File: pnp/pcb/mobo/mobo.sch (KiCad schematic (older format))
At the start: 19 parts, among them SW2 RESET

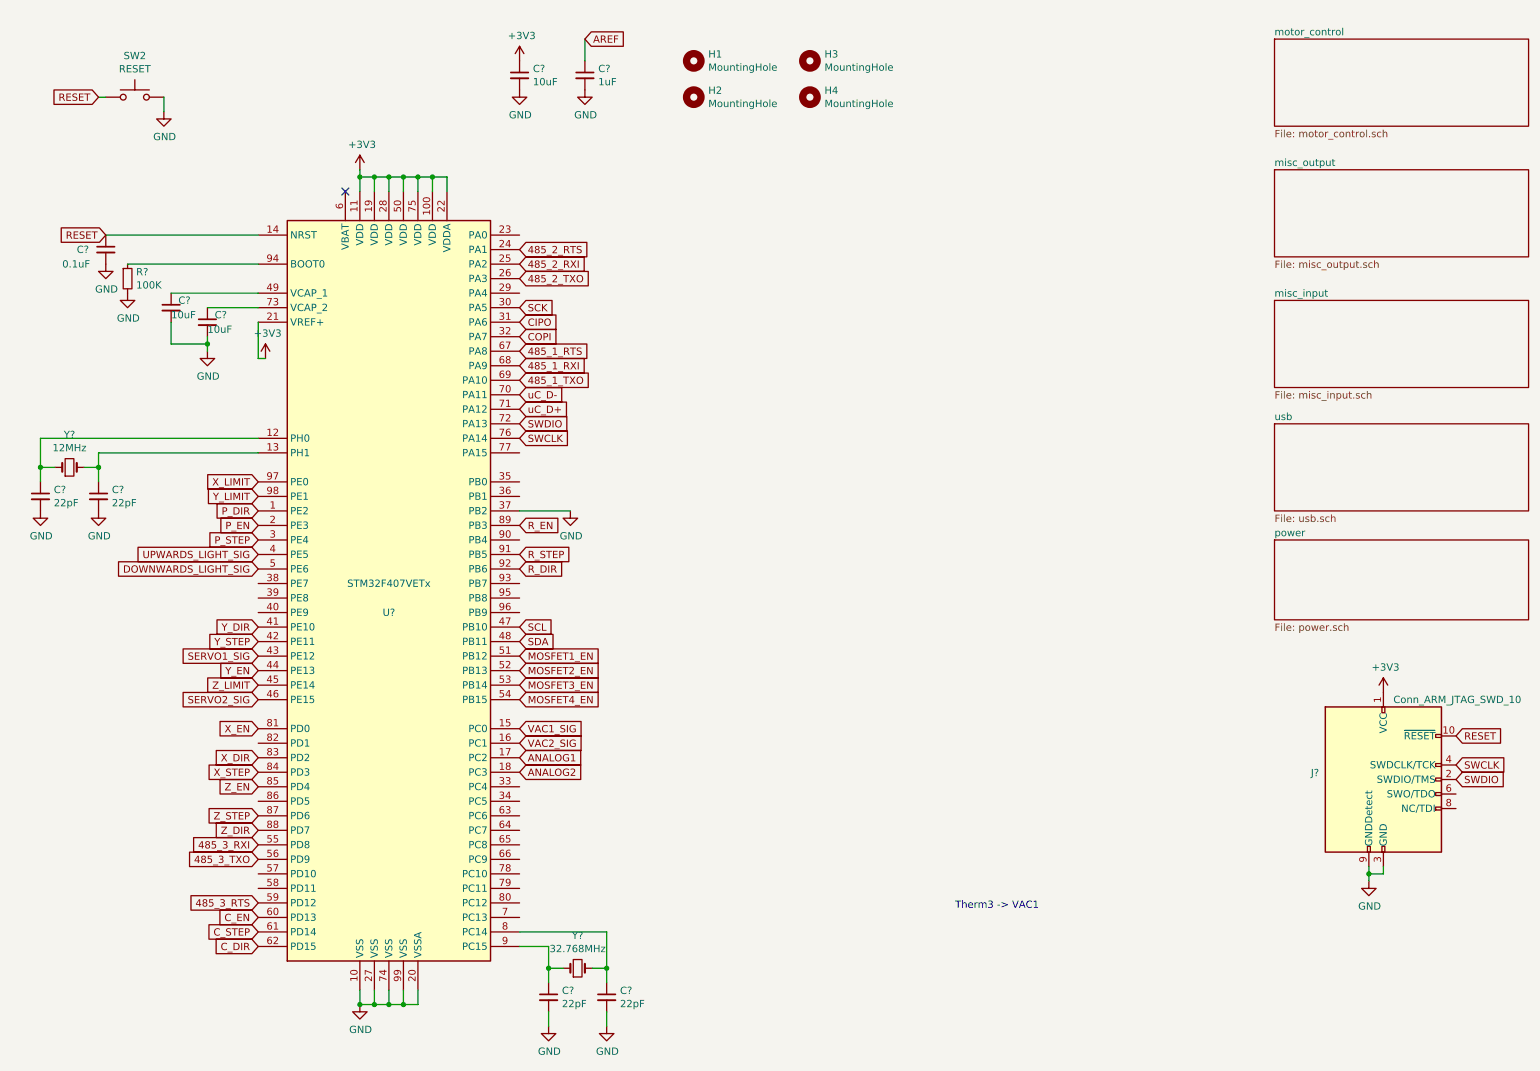
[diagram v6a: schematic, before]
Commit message: added spi to motor drivers
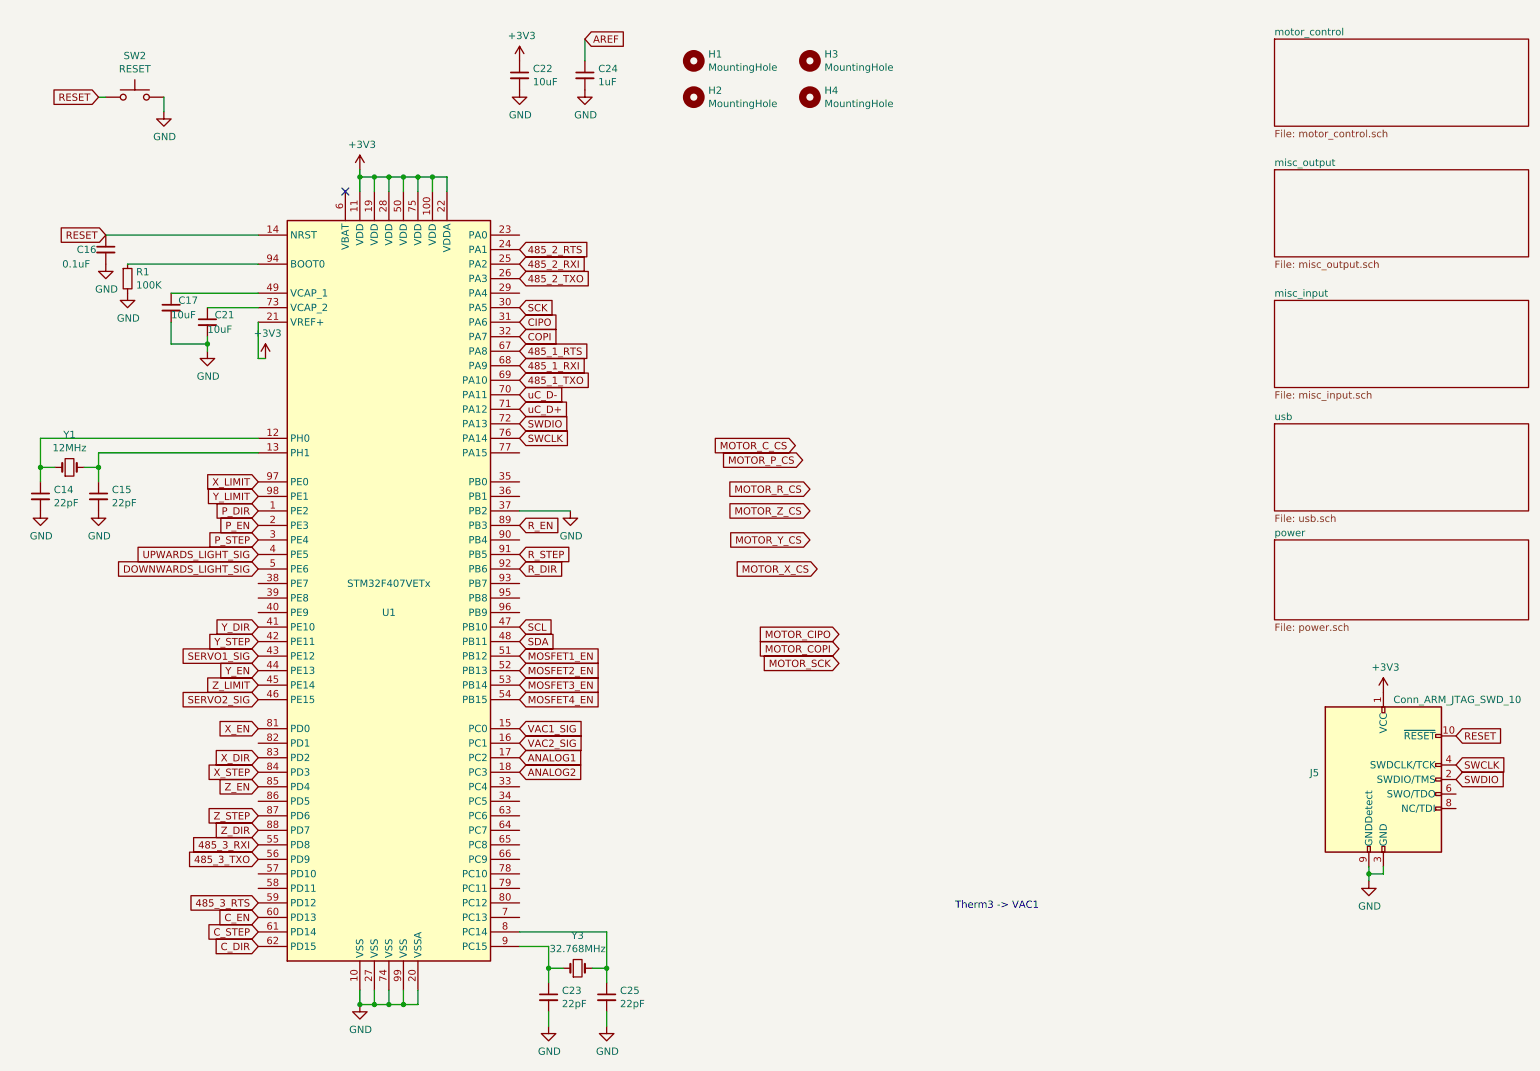
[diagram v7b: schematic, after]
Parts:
- R1: renamed from R?; footprint (none) -> Resistor_SMD:R_0805_2012Metric_Pad1.15x1.40mm_HandSolder
- Y1, Y3: renamed from Y?; footprint (none) -> Crystal:Crystal_SMD_0603-2Pin_6.0x3.5mm
- gave numbers to parts that had none: 11
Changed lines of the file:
@@
 R_EN
 $Comp
-L mobo-rescue:Conn_ARM_JTAG_SWD_10-Connector J?
+L mobo-rescue:Conn_ARM_JTAG_SWD_10-Connector J5
 U 1 1 5EEECA88
 P 9950 5750
-F 0 "J?" H 9507 5796 50  0000 R CNN
+F 0 "J5" H 9507 5796 50  0000 R CNN
 F 1 "Conn_ARM_JTAG_SWD_10" H 10900 6300 50  0000 R CNN
 F 2 "Connector_PinHeader_1.27mm:PinHeader_2x05_P1.27mm_Vertical_SMD" H 10000 5200 50  0001 L TNN
@@
 $EndComp
 $Comp
-L power:+3V3 #PWR?
+L power:+3V3 #PWR0114
 U 1 1 5EEF09A3
 P 2900 1550
-F 0 "#PWR?" H 2900 1400 50  0001 C CNN
+F 0 "#PWR0114" H 2900 1400 50  0001 C CNN
 F 1 "+3V3" H 2915 1723 50  0000 C CNN
 F 2 "" H 2900 1550 50  0001 C CNN
@@
 SWDIO
 $Comp
-L power:+3V3 #PWR?
+L power:+3V3 #PWR0115
 U 1 1 5EF002D9
 P 9950 5150
-F 0 "#PWR?" H 9950 5000 50  0001 C CNN
+F 0 "#PWR0115" H 9950 5000 50  0001 C CNN
 F 1 "+3V3" H 9965 5323 50  0000 C CNN
 F 2 "" H 9950 5150 50  0001 C CNN
@@
 $EndComp
 $Comp
-L power:GND #PWR?
+L power:GND #PWR0116
 U 1 1 5EF008CB
 P 9850 6450
-F 0 "#PWR?" H 9850 6200 50  0001 C CNN
+F 0 "#PWR0116" H 9850 6200 50  0001 C CNN
 F 1 "GND" H 9855 6277 50  0000 C CNN
 F 2 "" H 9850 6450 50  0001 C CNN
@@
 uC_D-
 $Comp
-L Device:C_Small C?
+L Device:C_Small C22
 U 1 1 5EF02584
 P 4000 900
-F 0 "C?" H 4092 946 50  0000 L CNN
+F 0 "C22" H 4092 946 50  0000 L CNN
 F 1 "10uF" H 4092 855 50  0000 L CNN
 F 2 "Capacitor_SMD:C_0805_2012Metric_Pad1.15x1.40mm_HandSolder" H 4000 900 50  0001 C CNN
@@
 $EndComp
 $Comp
-L power:+3V3 #PWR?
+L power:+3V3 #PWR0117
 U 1 1 5EF028FA
 P 4000 800
-F 0 "#PWR?" H 4000 650 50  0001 C CNN
+F 0 "#PWR0117" H 4000 650 50  0001 C CNN
 F 1 "+3V3" H 4015 973 50  0000 C CNN
 F 2 "" H 4000 800 50  0001 C CNN
@@
 $EndComp
 $Comp
-L power:GND #PWR?
+L power:GND #PWR0118
 U 1 1 5EF03055
 P 4000 1000
-F 0 "#PWR?" H 4000 750 50  0001 C CNN
+F 0 "#PWR0118" H 4000 750 50  0001 C CNN
 F 1 "GND" H 4005 827 50  0000 C CNN
 F 2 "" H 4000 1000 50  0001 C CNN
@@
 $EndComp
 $Comp
-L Device:C_Small C?
+L Device:C_Small C24
 U 1 1 5EF034CB
 P 4450 900
-F 0 "C?" H 4542 946 50  0000 L CNN
+F 0 "C24" H 4542 946 50  0000 L CNN
 F 1 "1uF" H 4542 855 50  0000 L CNN
 F 2 "Capacitor_SMD:C_0805_2012Metric_Pad1.15x1.40mm_HandSolder" H 4450 900 50  0001 C CNN
@@
 $EndComp
 $Comp
-L power:GND #PWR?
+L power:GND #PWR0119
 U 1 1 5EF0394F
 P 4450 1000
-F 0 "#PWR?" H 4450 750 50  0001 C CNN
+F 0 "#PWR0119" H 4450 750 50  0001 C CNN
 F 1 "GND" H 4455 827 50  0000 C CNN
 F 2 "" H 4450 1000 50  0001 C CNN
@@
 	3200 1600 3100 1600
 $Comp
-L MCU_ST_STM32F4:STM32F407VETx U?
+L MCU_ST_STM32F4:STM32F407VETx U1
 U 1 1 5EF214E8
 P 3100 4400
-F 0 "U?" H 3100 4200 50  0000 C CNN
+F 0 "U1" H 3100 4200 50  0000 C CNN
 F 1 "STM32F407VETx" H 3100 4400 50  0000 C CNN
 F 2 "Package_QFP:LQFP-100_14x14mm_P0.5mm" H 2400 1800 50  0001 R CNN
@@
 Connection ~ 3200 7300
 $Comp
-L Device:C_Small C?
+L Device:C_Small C16
 U 1 1 5F0CEC3B
 P 1150 2100
-F 0 "C?" H 950 2100 50  0000 L CNN
+F 0 "C16" H 950 2100 50  0000 L CNN
 F 1 "0.1uF" H 850 2000 50  0000 L CNN
 F 2 "Capacitor_SMD:C_0805_2012Metric_Pad1.15x1.40mm_HandSolder" H 1150 2100 50  0001 C CNN
@@
 	1150 2000 2200 2000
 $Comp
-L power:GND #PWR?
+L power:GND #PWR0120
 U 1 1 5F0CFA67
 P 1150 2200
-F 0 "#PWR?" H 1150 1950 50  0001 C CNN
+F 0 "#PWR0120" H 1150 1950 50  0001 C CNN
 F 1 "GND" H 1155 2027 50  0000 C CNN
 F 2 "" H 1150 2200 50  0001 C CNN
@@
 $EndComp
 $Comp
-L Device:R_Small R?
+L Device:R_Small R1
 U 1 1 5F0D0BAB
 P 1300 2300
-F 0 "R?" H 1359 2346 50  0000 L CNN
+F 0 "R1" H 1359 2346 50  0000 L CNN
 F 1 "100K" H 1359 2255 50  0000 L CNN
-F 2 "" H 1300 2300 50  0001 C CNN
+F 2 "Resistor_SMD:R_0805_2012Metric_Pad1.15x1.40mm_HandSolder" H 1300 2300 50  0001 C CNN
 F 3 "~" H 1300 2300 50  0001 C CNN
 	1    1300 2300
@@
 	1300 2200 2200 2200
 $Comp
-L power:GND #PWR?
+L power:GND #PWR0121
 U 1 1 5F0D3158
 P 1300 2400
-F 0 "#PWR?" H 1300 2150 50  0001 C CNN
+F 0 "#PWR0121" H 1300 2150 50  0001 C CNN
 F 1 "GND" H 1305 2227 50  0000 C CNN
 F 2 "" H 1300 2400 50  0001 C CNN
@@
 $EndComp
 $Comp
-L Device:C_Small C?
+L Device:C_Small C17
 U 1 1 5F0D3862
 P 1600 2500
-F 0 "C?" H 1650 2550 50  0000 L CNN
+F 0 "C17" H 1650 2550 50  0000 L CNN
 F 1 "10uF" H 1600 2450 50  0000 L CNN
 F 2 "Capacitor_SMD:C_0805_2012Metric_Pad1.15x1.40mm_HandSolder" H 1600 2500 50  0001 C CNN
@@
 $EndComp
 $Comp
-L Device:C_Small C?
+L Device:C_Small C21
 U 1 1 5F0D3CCF
 P 1850 2600
-F 0 "C?" H 1900 2650 50  0000 L CNN
+F 0 "C21" H 1900 2650 50  0000 L CNN
 F 1 "10uF" H 1850 2550 50  0000 L CNN
 F 2 "Capacitor_SMD:C_0805_2012Metric_Pad1.15x1.40mm_HandSolder" H 1850 2600 50  0001 C CNN
@@
 	1850 2500 2200 2500
 $Comp
-L power:GND #PWR?
+L power:GND #PWR0122
 U 1 1 5F0D9ED5
 P 1850 2800
-F 0 "#PWR?" H 1850 2550 50  0001 C CNN
+F 0 "#PWR0122" H 1850 2550 50  0001 C CNN
 F 1 "GND" H 1855 2627 50  0000 C CNN
 F 2 "" H 1850 2800 50  0001 C CNN
@@
 	1850 2750 1850 2700
 $Comp
-L power:GND #PWR?
+L power:GND #PWR0123
 U 1 1 5F0DF8B3
 P 4350 3900
-F 0 "#PWR?" H 4350 3650 50  0001 C CNN
+F 0 "#PWR0123" H 4350 3650 50  0001 C CNN
 F 1 "GND" H 4355 3727 50  0000 C CNN
 F 2 "" H 4350 3900 50  0001 C CNN
@@
 	4000 3900 4350 3900
 $Comp
-L Device:Crystal_Small Y?
+L Device:Crystal_Small Y1
 U 1 1 5F0E1806
 P 900 3600
-F 0 "Y?" H 900 3825 50  0000 C CNN
+F 0 "Y1" H 900 3825 50  0000 C CNN
 F 1 "12MHz" H 900 3734 50  0000 C CNN
-F 2 "" H 900 3600 50  0001 C CNN
+F 2 "Crystal:Crystal_SMD_0603-2Pin_6.0x3.5mm" H 900 3600 50  0001 C CNN
 F 3 "~" H 900 3600 50  0001 C CNN
 	1    900  3600
@@
 $EndComp
 $Comp
-L Device:Crystal_Small Y?
+L Device:Crystal_Small Y3
 U 1 1 5F0E266F
 P 4400 7050
-F 0 "Y?" H 4400 7275 50  0000 C CNN
+F 0 "Y3" H 4400 7275 50  0000 C CNN
 F 1 "32.768MHz" H 4400 7184 50  0000 C CNN
-F 2 "" H 4400 7050 50  0001 C CNN
+F 2 "Crystal:Crystal_SMD_0603-2Pin_6.0x3.5mm" H 4400 7050 50  0001 C CNN
 F 3 "~" H 4400 7050 50  0001 C CNN
 	1    4400 7050
@@
 $EndComp
 $Comp
-L Device:C_Small C?
+L Device:C_Small C25
 U 1 1 5F0E33A4
 P 4600 7250
-F 0 "C?" H 4692 7296 50  0000 L CNN
+F 0 "C25" H 4692 7296 50  0000 L CNN
 F 1 "22pF" H 4692 7205 50  0000 L CNN
 F 2 "Capacitor_SMD:C_0805_2012Metric_Pad1.15x1.40mm_HandSolder" H 4600 7250 50  0001 C CNN
@@
 $EndComp
 $Comp
-L Device:C_Small C?
+L Device:C_Small C23
 U 1 1 5F0E4761
 P 4200 7250
-F 0 "C?" H 4292 7296 50  0000 L CNN
+F 0 "C23" H 4292 7296 50  0000 L CNN
 F 1 "22pF" H 4292 7205 50  0000 L CNN
 F 2 "Capacitor_SMD:C_0805_2012Metric_Pad1.15x1.40mm_HandSolder" H 4200 7250 50  0001 C CNN
@@
 	4600 7050 4600 7150
 $Comp
-L power:GND #PWR?
+L power:GND #PWR0124
 U 1 1 5F0E65D5
 P 4200 7450
-F 0 "#PWR?" H 4200 7200 50  0001 C CNN
+F 0 "#PWR0124" H 4200 7200 50  0001 C CNN
 F 1 "GND" H 4205 7277 50  0000 C CNN
 F 2 "" H 4200 7450 50  0001 C CNN
@@
 $EndComp
 $Comp
-L power:GND #PWR?
+L power:GND #PWR0125
 U 1 1 5F0E6A2C
 P 4600 7450
-F 0 "#PWR?" H 4600 7200 50  0001 C CNN
+F 0 "#PWR0125" H 4600 7200 50  0001 C CNN
 F 1 "GND" H 4605 7277 50  0000 C CNN
 F 2 "" H 4600 7450 50  0001 C CNN
@@
 Connection ~ 4600 7050
 $Comp
-L Device:C_Small C?
+L Device:C_Small C15
 U 1 1 5F0F0EE5
 P 1100 3800
-F 0 "C?" H 1192 3846 50  0000 L CNN
+F 0 "C15" H 1192 3846 50  0000 L CNN
 F 1 "22pF" H 1192 3755 50  0000 L CNN
 F 2 "Capacitor_SMD:C_0805_2012Metric_Pad1.15x1.40mm_HandSolder" H 1100 3800 50  0001 C CNN
@@
 $EndComp
 $Comp
-L Device:C_Small C?
+L Device:C_Small C14
 U 1 1 5F10974E
 P 700 3800
-F 0 "C?" H 792 3846 50  0000 L CNN
+F 0 "C14" H 792 3846 50  0000 L CNN
 F 1 "22pF" H 792 3755 50  0000 L CNN
 F 2 "Capacitor_SMD:C_0805_2012Metric_Pad1.15x1.40mm_HandSolder" H 700 3800 50  0001 C CNN
@@
 Connection ~ 700  3600
 $Comp
-L power:GND #PWR?
+L power:GND #PWR0126
 U 1 1 5F111B2A
 P 700 3900
-F 0 "#PWR?" H 700 3650 50  0001 C CNN
+F 0 "#PWR0126" H 700 3650 50  0001 C CNN
 F 1 "GND" H 705 3727 50  0000 C CNN
 F 2 "" H 700 3900 50  0001 C CNN
@@
 $EndComp
 $Comp
-L power:GND #PWR?
+L power:GND #PWR0127
 U 1 1 5F112138
 P 1100 3900
-F 0 "#PWR?" H 1100 3650 50  0001 C CNN
+F 0 "#PWR0127" H 1100 3650 50  0001 C CNN
 F 1 "GND" H 1105 3727 50  0000 C CNN
 F 2 "" H 1100 3900 50  0001 C CNN
@@
 NoConn ~ 2800 1700
 $Comp
-L power:+3V3 #PWR?
+L power:+3V3 #PWR0128
 U 1 1 5F115D16
 P 2250 2850
-F 0 "#PWR?" H 2250 2700 50  0001 C CNN
+F 0 "#PWR0128" H 2250 2700 50  0001 C CNN
 F 1 "+3V3" H 2265 3023 50  0000 C CNN
 F 2 "" H 2250 2850 50  0001 C CNN
@@
 Text GLabel 2200 6600 0    50   Input ~ 0
 485_3_RTS
+Text GLabel 6200 4750 0    50   Input ~ 0
+MOTOR_CIPO
+Text GLabel 6200 4850 0    50   Input ~ 0
+MOTOR_COPI
+Text GLabel 6200 4950 0    50   Input ~ 0
+MOTOR_SCK
+Text GLabel 6050 4300 0    50   Input ~ 0
+MOTOR_X_CS
+Text GLabel 6000 4100 0    50   Input ~ 0
+MOTOR_Y_CS
+Text GLabel 6000 3900 0    50   Input ~ 0
+MOTOR_Z_CS
+Text GLabel 6000 3750 0    50   Input ~ 0
+MOTOR_R_CS
+Text GLabel 5950 3550 0    50   Input ~ 0
+MOTOR_P_CS
+Text GLabel 5900 3450 0    50   Input ~ 0
+MOTOR_C_CS
 $EndSCHEMATC
